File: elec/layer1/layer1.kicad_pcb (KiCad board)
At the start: 2 copper layers, 178 x 173.3 mm, 77 parts, among them U1 DEV-15583, U2 CD74HC4067SM, U3 CD74HC4067SM

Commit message: almost done maybe
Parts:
- removed BoosCaps1, BoostCaps1: Conn_01x05, Pinheaders:PinHeader_1x05_P2.54mm_Vertical
- removed the Boost1 at (323.2, 161.3)
- removed the Boost2 at (323.2, 126.6)
- added H1: MountingHole, MountingHole:MountingHole_2.2mm_M2_DIN965_Pad_TopBottom, F.Cu at (198.2, 218.2)
- added H10: MountingHole, MountingHole:MountingHole_3.2mm_M3_DIN965_Pad_TopBottom, F.Cu at (227.8, 103.4)
- added H11: MountingHole, MountingHole:MountingHole_3.2mm_M3_DIN965_Pad_TopBottom, F.Cu at (233.1, 77.5)
- added H12: MountingHole, MountingHole:MountingHole_3.2mm_M3_DIN965_Pad_TopBottom, F.Cu at (163.4, 77.5)
- added H13: MountingHole, MountingHole:MountingHole_3.2mm_M3_DIN965_Pad_TopBottom, F.Cu at (168.7, 103.4)
- added H14: MountingHole, MountingHole:MountingHole_3.2mm_M3_DIN965_Pad_TopBottom, F.Cu at (148.9, 123.2)
- added H15: MountingHole, MountingHole:MountingHole_3.2mm_M3_DIN965_Pad_TopBottom, F.Cu at (122.9, 117.9)
- added H16: MountingHole, MountingHole:MountingHole_3.2mm_M3_DIN965_Pad_TopBottom, F.Cu at (122.9, 187.7)
- added H17: MountingHole, MountingHole:MountingHole_3.2mm_M3_DIN965_Pad_TopBottom, F.Cu at (148.9, 182.4)
- added H18: MountingHole, MountingHole:MountingHole_3.2mm_M3_DIN965_Pad_TopBottom, F.Cu at (168.7, 202.2)
- added H19: MountingHole, MountingHole:MountingHole_3.2mm_M3_DIN965_Pad_TopBottom, F.Cu at (165.3, 229.0)
- added H2: MountingHole, MountingHole:MountingHole_2.2mm_M2_DIN965_Pad_TopBottom, F.Cu at (198.2, 188.2)
- added H20: MountingHole, MountingHole:MountingHole_3.2mm_M3_DIN965_Pad_TopBottom, F.Cu at (185.7, 218.2)
- added H21: MountingHole, MountingHole:MountingHole_3.2mm_M3_DIN965_Pad_TopBottom, F.Cu at (185.7, 193.2)
- added H22: MountingHole, MountingHole:MountingHole_3.2mm_M3_DIN965_Pad_TopBottom, F.Cu at (210.5, 193.3)
- added H23: MountingHole, MountingHole:MountingHole_3.2mm_M3_DIN965_Pad_TopBottom, F.Cu at (237.7, 175.3)
- added H24: MountingHole, MountingHole:MountingHole_3.2mm_M3_DIN965_Pad_TopBottom, F.Cu at (238.2, 130.3)
- added H25: MountingHole, MountingHole:MountingHole_3.2mm_M3_DIN965_Pad_TopBottom, F.Cu at (208.2, 110.8)
- added H26: MountingHole, MountingHole:MountingHole_3.2mm_M3_DIN965_Pad_TopBottom, F.Cu at (208.2, 130.9)
- added H27: MountingHole, MountingHole:MountingHole_3.2mm_M3_DIN965_Pad_TopBottom, F.Cu at (202.2, 162.8)
- added H28: MountingHole, MountingHole:MountingHole_3.2mm_M3_DIN965_Pad_TopBottom, F.Cu at (194.2, 162.8)
- added H29: MountingHole, MountingHole:MountingHole_3.2mm_M3_DIN965_Pad_TopBottom, F.Cu at (202.2, 142.8)
- added H3: MountingHole, MountingHole:MountingHole_3.2mm_M3_DIN965_Pad_TopBottom, F.Cu at (210.7, 218.2)
- added H30: MountingHole, MountingHole:MountingHole_3.2mm_M3_DIN965_Pad_TopBottom, F.Cu at (194.2, 142.8)
- added H31: MountingHole, MountingHole:MountingHole_3.2mm_M3_DIN965_Pad_TopBottom, F.Cu at (188.2, 130.9)
- added H32: MountingHole, MountingHole:MountingHole_3.2mm_M3_DIN965_Pad_TopBottom, F.Cu at (188.2, 110.9)
- added H33: MountingHole, MountingHole:MountingHole_3.2mm_M3_DIN965_Pad_TopBottom, F.Cu at (158.2, 130.3)
- added H34: MountingHole, MountingHole:MountingHole_3.2mm_M3_DIN965_Pad_TopBottom, F.Cu at (158.2, 175.3)
- added H4: MountingHole, MountingHole:MountingHole_3.2mm_M3_DIN965_Pad_TopBottom, F.Cu at (231.2, 229.0)
- added H5: MountingHole, MountingHole:MountingHole_3.2mm_M3_DIN965_Pad_TopBottom, F.Cu at (227.8, 202.2)
- added H6: MountingHole, MountingHole:MountingHole_3.2mm_M3_DIN965_Pad_TopBottom, F.Cu at (247.6, 182.4)
- added H7: MountingHole, MountingHole:MountingHole_3.2mm_M3_DIN965_Pad_TopBottom, F.Cu at (273.6, 187.7)
- added H8: MountingHole, MountingHole:MountingHole_3.2mm_M3_DIN965_Pad_TopBottom, F.Cu at (273.6, 117.9)
- added H9: MountingHole, MountingHole:MountingHole_3.2mm_M3_DIN965_Pad_TopBottom, F.Cu at (247.6, 123.2)
- added L1-->L2Connection1: Conn_01x08, L1:PinHeader_1x08_P2.54mm_Vertical, F.Cu at (175.5, 73.7)
- added L1-->L2Connection2: Conn_01x08, L1:PinHeader_1x08_P2.54mm_Vertical, F.Cu at (218.2, 73.6)
- added Modules Normal**: Modules, Modules(Normal):Modules, F.Cu at (129.0, 153.2)
- added Modules Normal**: Modules, Modules(Normal):Modules, F.Cu at (267.5, 153.1)
- moved U1 180.4 mm to (198.2, 85.1), turned to -90 degrees
- moved Solactivation2 107.8 mm to (260.1, 135.5), turned to 90 degrees
- moved Solactivation1 85.9 mm to (260.1, 170.2), turned to 90 degrees
- moved Boost1 1.27 mm to (120.1, 170.5)
- moved Boost2 1.27 mm to (120.1, 135.8)
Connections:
- U1 pad 18: /Mux Com (1-16) -> /Mux Com (17-32)
- U1 pad 19: /Mux Com (17-32) -> /Mux Com (1-16)
- U1 pad 2: /Sol -> unconnected-(U1-Pad2)
- U1 pad 20: unconnected-(U1-Pad20) -> /Sol
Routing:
- net /S0: track 0.00 -> 31.2 mm, vias 0 -> 2
- net /S2: track 0.00 -> 30.0 mm, vias 0 -> 2
- net /S3: track 0.35 -> 24.5 mm, vias 0 -> 2
- net /S1: track 0.95 -> 24.5 mm
- net Net-(U2-I6): track 41.9 -> 39.5 mm
- net Net-(U2-I11): track 46.2 -> 48.1 mm, vias 0 -> 2
- net Net-(U2-I1): track 50.5 -> 51.9 mm
- net Net-(U3-I13): track 49.6 -> 48.3 mm
- net Net-(U3-I15): track 46.1 -> 47.4 mm
- net Net-(U3-I14): track 48.1 -> 46.9 mm
- net Net-(U3-I11): track 51.7 -> 50.6 mm
- net Net-(U3-I3): track 47.0 -> 46.1 mm
- net Net-(U3-I4): track 50.9 -> 50.0 mm
- net Net-(U3-I12): track 49.3 -> 48.4 mm
- net Net-(U2-I7): track 38.2 -> 37.5 mm
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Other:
- board size 178 x 173.3 mm -> 178 x 178 mm
- board text added: "Boost"
- board text added: "Solactivation"

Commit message: l1:connected most stuff
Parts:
- moved L1-->L2Connection1 44.3 mm to (219.8, 73.1), turned to -90 degrees
- moved L1-->L2Connection2 41.5 mm to (176.7, 73.1), turned to 90 degrees
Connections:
- L1-->L2Connection1 pad 4: unconnected-(L1--&gt;L2Connection1-Pin_4-Pad4) -> +5V
- L1-->L2Connection1 pad 5: unconnected-(L1--&gt;L2Connection1-Pin_5-Pad5) -> +5V
- U1 pad 7: unconnected-(U1-Pad7) -> /TX
- U1 pad 8: unconnected-(U1-Pad8) -> /RX
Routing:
- net +12V: track 0.00 -> 292.9 mm
- net +24V: track 0.00 -> 157.1 mm
- net +3V3: track 3.53 -> 150.6 mm, vias 7 -> 0
- net /Mux Com (17-32): track 0.00 -> 133.5 mm, vias 0 -> 1
- net /Sol: track 0.00 -> 108.3 mm
- net /Mux Com (1-16): track 0.00 -> 75.6 mm, vias 0 -> 1
- net /S3: track 24.5 -> 99.6 mm, vias 2 -> 4
- net /S0: track 31.2 -> 93.8 mm, vias 2 -> 4
- net /S1: track 24.5 -> 83.9 mm, vias 0 -> 1
- net /S2: track 30.0 -> 87.4 mm
- net +5V: track 0.00 -> 45.6 mm
- net /TX: track 0.00 -> 9.39 mm
- net /RX: track 0.00 -> 9.39 mm
- net Net-(U2-I8): track 38.0 -> 37.9 mm, vias 0 -> 2
- net Net-(U3-I8): vias 0 -> 2
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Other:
- board size 178 x 178 mm -> 178 x 173.3 mm

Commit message: fix: layer1 pcb
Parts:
- moved U1 2.20 mm to (198.2, 87.3)
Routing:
- net +3V3: track 150.6 -> 124.8 mm
- net +5V: track 45.6 -> 36.4 mm
- net /S1: track 83.9 -> 81.6 mm
- net /S0: track 93.8 -> 91.6 mm
- net /S3: track 99.6 -> 97.4 mm
- net /Mux Com (17-32): track 133.5 -> 131.3 mm
- net /Mux Com (1-16): track 75.6 -> 73.4 mm
- net /S2: track 87.4 -> 85.2 mm
- net /RX: track 9.39 -> 11.3 mm
- net /TX: track 9.39 -> 11.0 mm
- net /Sol: track 108.3 -> 107.4 mm
- net Net-(U2-I15): track 47.9 -> 48.4 mm
- net GND: vias 68 -> 74
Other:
- board text added: "12v"
- board text added: "3v3"
- board text added: "5v"
- board text added: "Gnd"
- board text added: "Rx"
- board text added: "Teensy 4.0"
- board text added: "Tx"
- board text added: "Vent Exhaust"

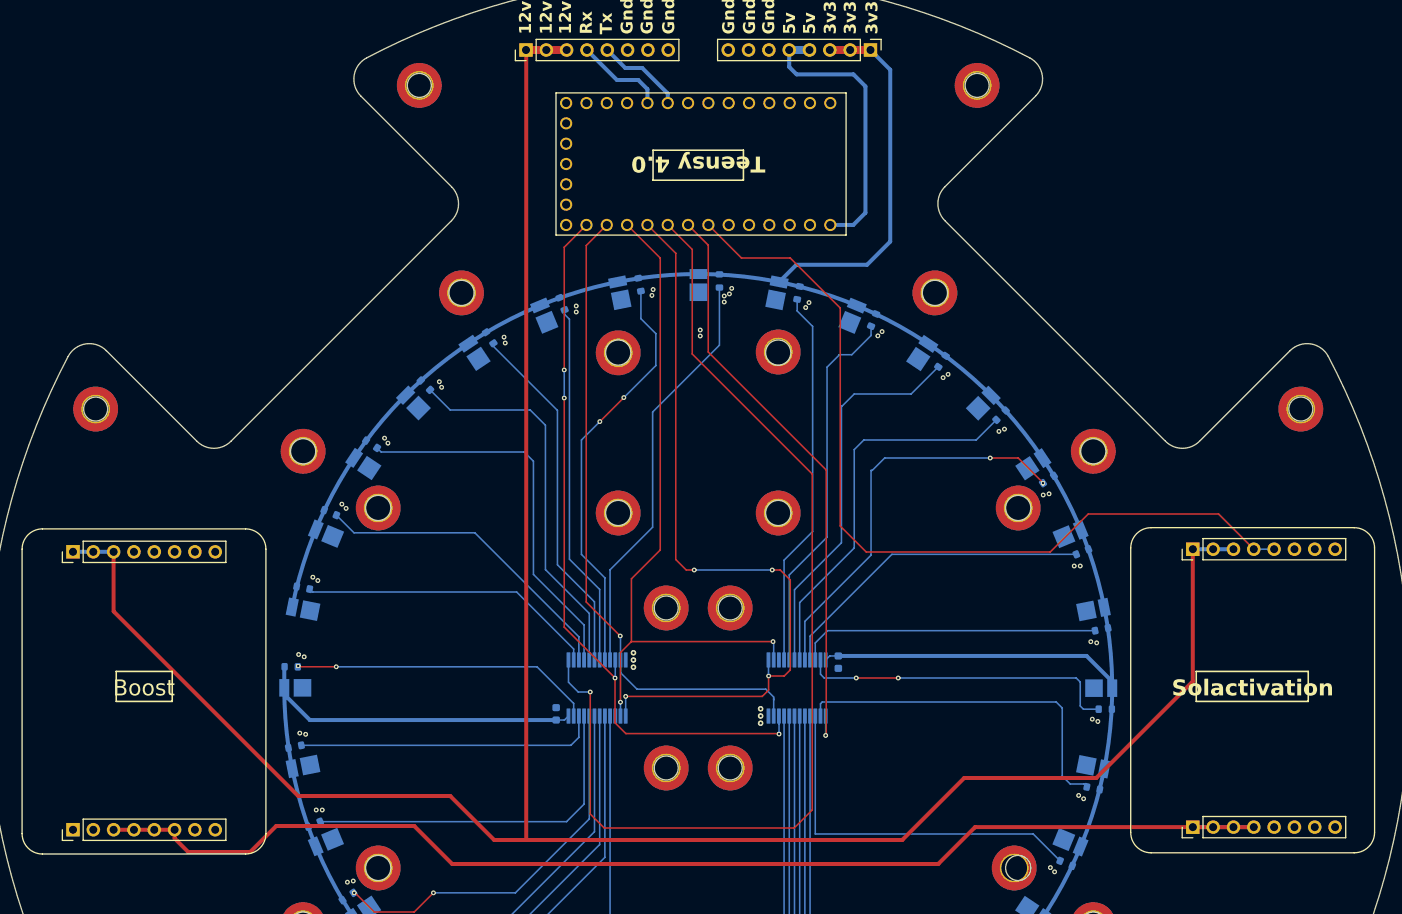
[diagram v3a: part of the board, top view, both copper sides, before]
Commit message: l1: added some stuff havent connected data to drivers yet
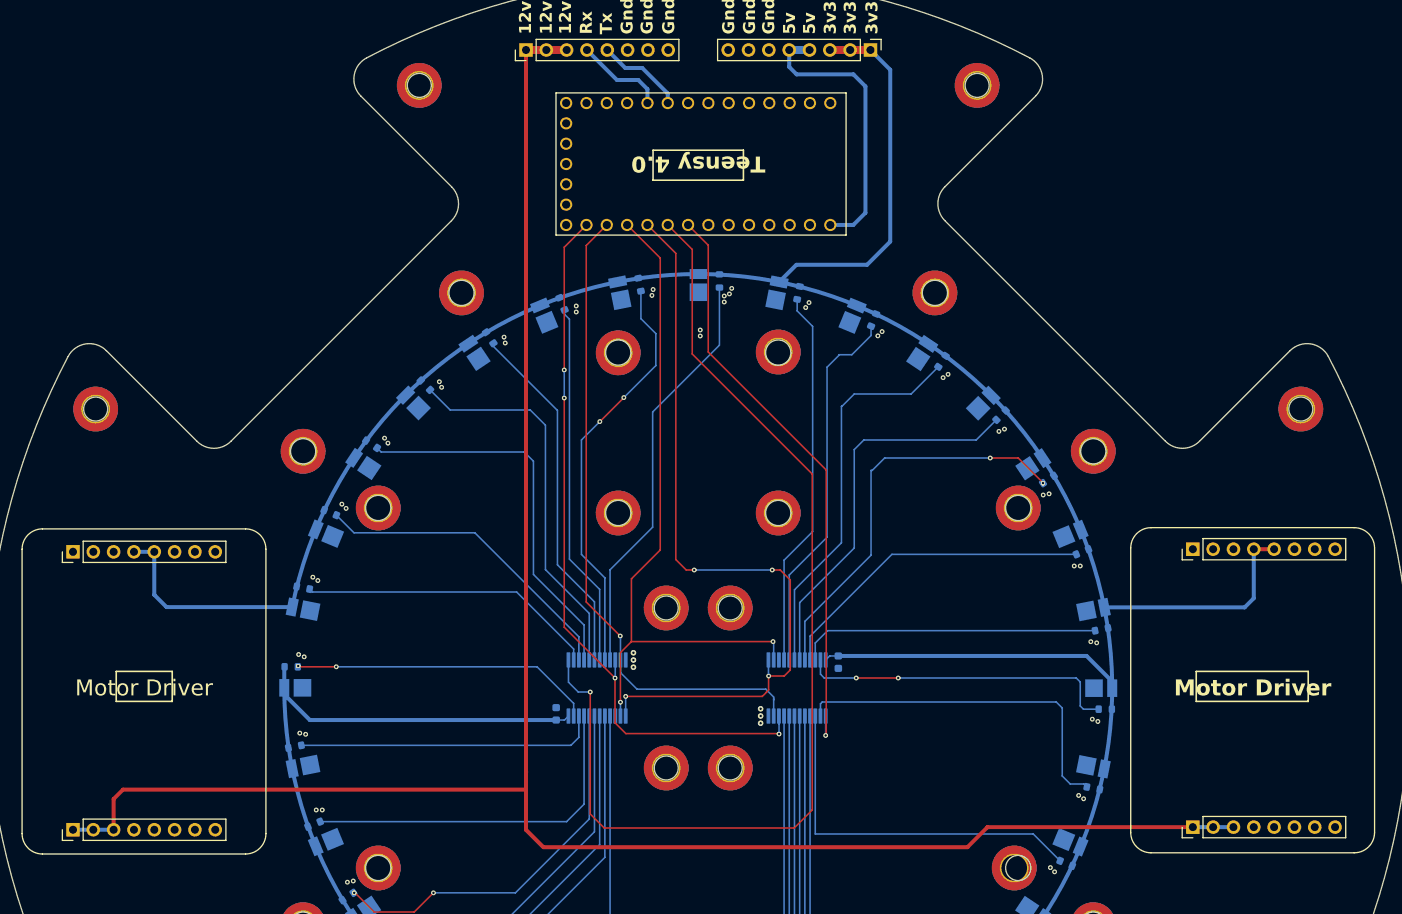
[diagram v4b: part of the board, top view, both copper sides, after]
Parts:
- removed Boost1, Boost2, Solactivation1, Solactivation2: Conn_01x08, L1:PinHeader_1x08_P2.54mm_Vertical
- added Driver1: Conn_01x08, Pinheaders:PinHeader_1x08_P2.54mm_Vertical, F.Cu at (260.1, 135.5)
- added Driver2: Conn_01x08, Pinheaders:PinHeader_1x08_P2.54mm_Vertical, F.Cu at (260.1, 170.2)
- added Driver3: Conn_01x08, Pinheaders:PinHeader_1x08_P2.54mm_Vertical, F.Cu at (120.1, 135.8)
- added Driver4: Conn_01x08, Pinheaders:PinHeader_1x08_P2.54mm_Vertical, F.Cu at (120.1, 170.5)
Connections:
- U1 pad 3.3V_1: +3V3 -> unconnected-(U1-Pad3.3V_1)
- U1 pad 3.3V_2: +3V3 -> unconnected-(U1-Pad3.3V_2)
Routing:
- net +24V: track 157.1 -> 0.00 mm
- net /Sol: track 107.4 -> 0.00 mm
- net +3V3: track 124.8 -> 178.4 mm
- net +12V: track 292.9 -> 254.4 mm
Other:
- board text added: "Motor Driver"
- board text removed: "Boost"
- board text removed: "Solactivation"

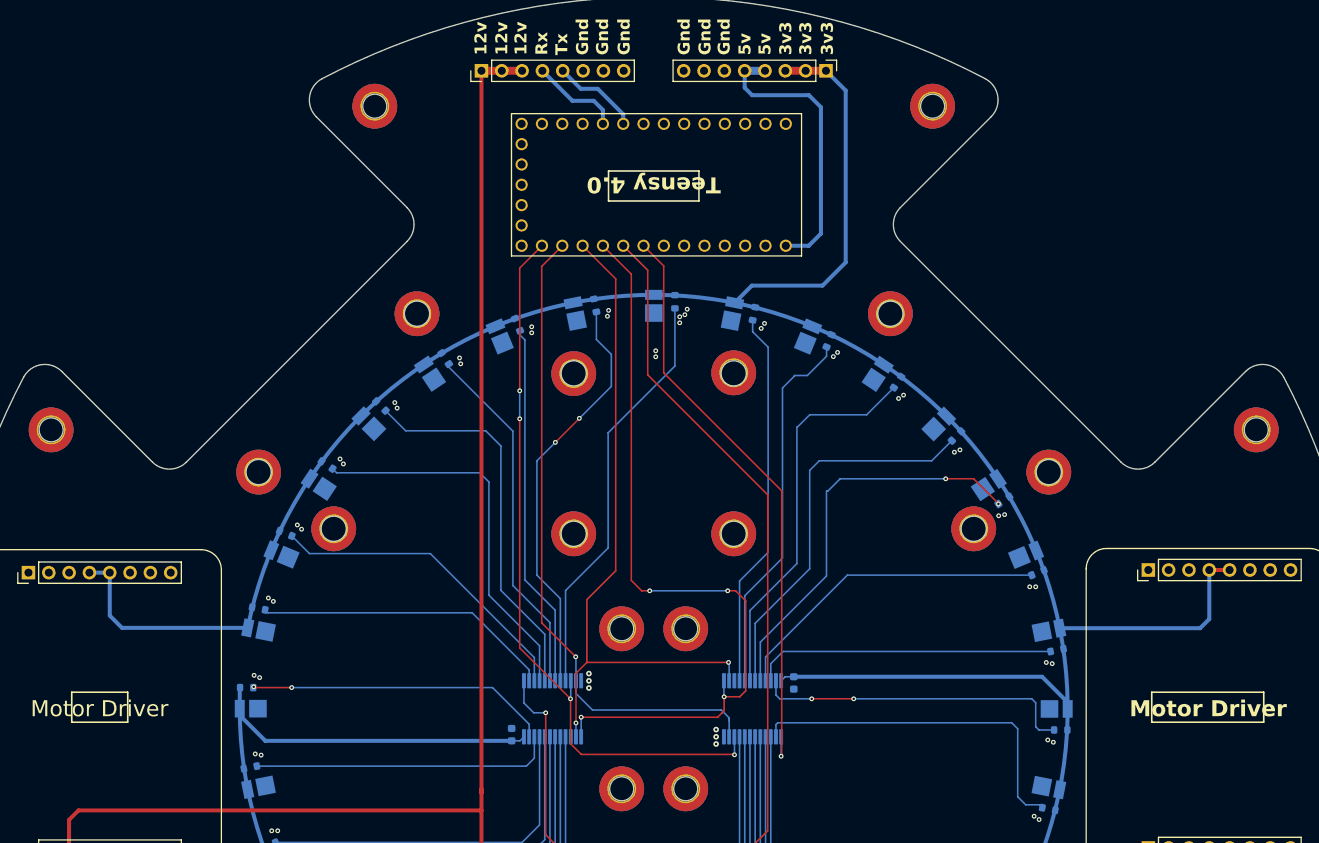
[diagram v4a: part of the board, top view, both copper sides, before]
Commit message: connectred the pins for driver
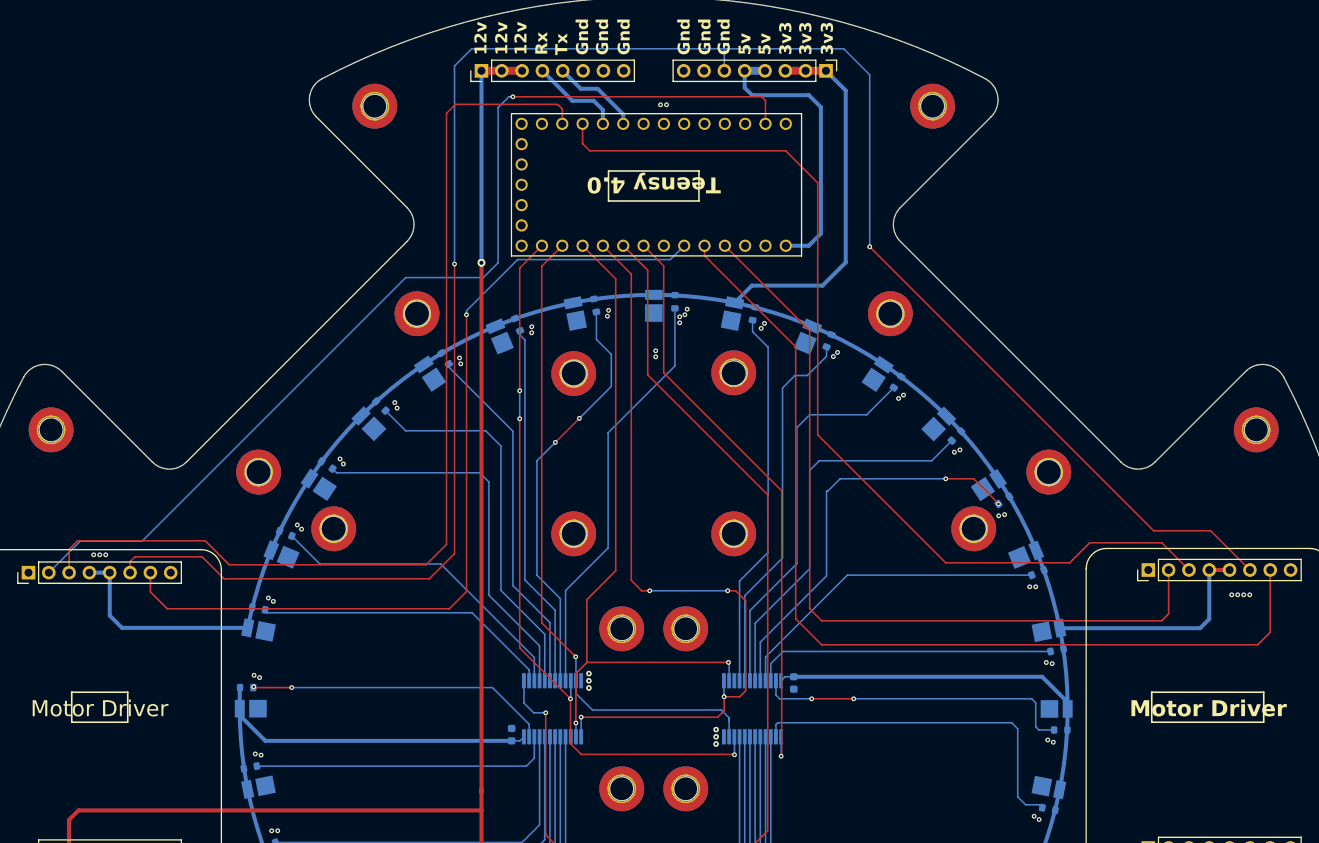
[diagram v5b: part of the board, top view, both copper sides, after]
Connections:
- Driver1 pad 2: /M IN B -> /M1 IN B
- Driver1 pad 3: /M PWM -> /M1 PWM
- Driver1 pad 7: /M IN A -> /M1 IN A
- Driver3 pad 2: /M IN B -> /M2 IN B
- Driver3 pad 3: /M PWM -> /M2 PWM
- Driver3 pad 7: /M IN A -> /M2 IN A
- L1-->L2Connection1 pad 6: GND -> /M SW
- U1 pad 0: unconnected-(U1-Pad0) -> /M2 IN B
- U1 pad 10: unconnected-(U1-Pad10) -> /M2 PWM
- U1 pad 21: unconnected-(U1-Pad21) -> /M2 IN A
- U1 pad 22: unconnected-(U1-Pad22) -> /M1 IN A
- U1 pad 23: unconnected-(U1-Pad23) -> /M1 IN B
- U1 pad 9: unconnected-(U1-Pad9) -> /M1 PWM
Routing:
- net /M SW: track 0.00 -> 248.3 mm, vias 0 -> 2
- net /M2 IN B: track 0.00 -> 128.7 mm, vias 0 -> 1
- net /M2 PWM: track 0.00 -> 123.7 mm
- net /M1 PWM: track 0.00 -> 120.9 mm
- net /M1 IN A: track 0.00 -> 120.4 mm
- net /M2 IN A: track 0.00 -> 109.4 mm, vias 0 -> 1
- net /M1 IN B: track 0.00 -> 101.1 mm
- net +12V: vias 0 -> 1
- net GND: vias 74 -> 83

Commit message: driver jsts r almost done ig
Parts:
- removed L1-->L2Connection1: Conn_01x08, L1:PinHeader_1x08_P2.54mm_Vertical
- added Driver5: Conn_01x08, Pinheaders:PinHeader_1x08_P2.54mm_Vertical, F.Cu at (76.3, 111.2)
- added Driver6: Conn_01x08, Pinheaders:PinHeader_1x08_P2.54mm_Vertical, F.Cu at (258.7, 175.3)
- added Driver7: Conn_01x08, Pinheaders:PinHeader_1x08_P2.54mm_Vertical, F.Cu at (120.1, 130.8)
- added Driver8: Conn_01x08, Pinheaders:PinHeader_1x08_P2.54mm_Vertical, F.Cu at (120.0, 175.4)
- moved L1-->L2Connection2 12.1 mm to (188.6, 75.2)
- moved Driver2 1.40 mm to (258.7, 170.1)
- moved Driver1 1.40 mm to (258.7, 135.5)
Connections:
- L1-->L2Connection2 pad 1: +12V -> +5V
- L1-->L2Connection2 pad 2: +12V -> +5V
- L1-->L2Connection2 pad 3: +12V -> unconnected-(L1--&gt;L2Connection2-Pin_3-Pad3)
- U1 pad 0: /M2 IN B -> unconnected-(U1-Pad0)
- U1 pad 10: /M2 PWM -> unconnected-(U1-Pad10)
- U1 pad 19: /Mux Com (1-16) -> unconnected-(U1-Pad19)
- U1 pad 20: /Sol -> unconnected-(U1-Pad20)
- U1 pad 21: /M2 IN A -> unconnected-(U1-Pad21)
- U1 pad 22: /M1 IN A -> unconnected-(U1-Pad22)
- U1 pad 23: /M1 IN B -> unconnected-(U1-Pad23)
- U1 pad 9: /M1 PWM -> unconnected-(U1-Pad9)
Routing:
- net /M SW: track 248.3 -> 4.99 mm, vias 2 -> 0
- net +12V: track 254.4 -> 30.5 mm, vias 1 -> 0
- net /M2 IN B: track 128.7 -> 4.99 mm, vias 1 -> 0
- net /M1 PWM: track 120.9 -> 0.00 mm
- net /M1 IN A: track 120.4 -> 0.00 mm
- net /M2 PWM: track 123.7 -> 4.99 mm
- net /M2 IN A: track 109.4 -> 4.99 mm, vias 1 -> 0
- net /M1 IN B: track 101.1 -> 0.00 mm
- net +3V3: track 178.4 -> 130.3 mm
- net unconnected-(U1-Pad21): track 0.00 -> 21.5 mm
- net +5V: track 36.4 -> 53.4 mm
- net /RX: track 11.3 -> 6.29 mm
- net /TX: track 11.0 -> 6.29 mm
- net unconnected-(U1-Pad9): track 0.00 -> 3.74 mm
- net unconnected-(U1-Pad22): track 0.00 -> 1.23 mm
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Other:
- board text removed: "12v"
- board text removed: "5v"
- board text removed: "Gnd"
- board text removed: "Rx"
- board text removed: "Tx"
